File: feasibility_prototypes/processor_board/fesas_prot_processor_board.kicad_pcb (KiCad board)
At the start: 2 copper layers, 89 x 91 mm, 21 parts, among them P1 CONN_01X08, P10 CONN_01X02, P2 CONN_01X08, P3 CONN_01X02, P4 CONN_01X06, P5 CONN_01X08, P6 CONN_01X08, P7 CONN_01X08, P8 CONN_01X08, P9 CONN_01X02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

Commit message: Addded guard trace for cap-sense pad
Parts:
- added R5: R, Resistors_SMD:R_0805_HandSoldering, F.Cu at (197.5, 59.1)
- added R6: R, Resistors_SMD:R_0805_HandSoldering, F.Cu at (197.5, 66.7)
- added SW1: NKKswitches_G3T22AP, med_conn_prototype_footprints:NKKSwitches_G3T22AP, F.Cu at (191.8, 62.9)
- moved P9 14.5 mm to (181.0, 41.3)
- moved P4 12.1 mm to (198.8, 41.3)
- moved P10 7.85 mm to (172.7, 56.5)
- moved C3 4.58 mm to (191.8, 82.5)
- moved P2 3.81 mm to (191.8, 115.6)
- moved P5 3.81 mm to (161.3, 100.3)
- moved P1 1.27 mm to (125.7, 69.8)
- moved P3 0.63 mm to (160.0, 41.3)
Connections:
- U1 pad 27: /PGC(ICSPCLK) -> Net-(SW1-Pad2)
- U1 pad 28: /PGD(ICSPDAT) -> Net-(SW1-Pad5)
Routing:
- net /Guard_trace: track 0.00 -> 101.2 mm
- net Net-(SW1-Pad5): track 0.00 -> 31.4 mm
- net Net-(SW1-Pad2): track 0.00 -> 26.6 mm
- net /PGD(ICSPDAT): track 39.1 -> 23.2 mm
- net /MCLR/Vpp: track 74.3 -> 84.4 mm
- net Net-(P10-Pad2): track 25.8 -> 35.3 mm
- net /PGC(ICSPCLK): track 44.5 -> 35.8 mm
- net Net-(R5-Pad2): track 0.00 -> 8.19 mm
- net Net-(R6-Pad1): track 0.00 -> 6.91 mm
- net Net-(P2-Pad8): track 48.9 -> 53.4 mm
- net Net-(P2-Pad6): track 53.6 -> 58.0 mm
- net Net-(P2-Pad4): track 58.2 -> 62.7 mm
- net Net-(P5-Pad5): track 36.3 -> 40.1 mm
- net Net-(P5-Pad3): track 36.4 -> 40.2 mm
- net GND: track 57.4 -> 59.5 mm
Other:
- board size 89 x 91 mm -> 95 x 91 mm

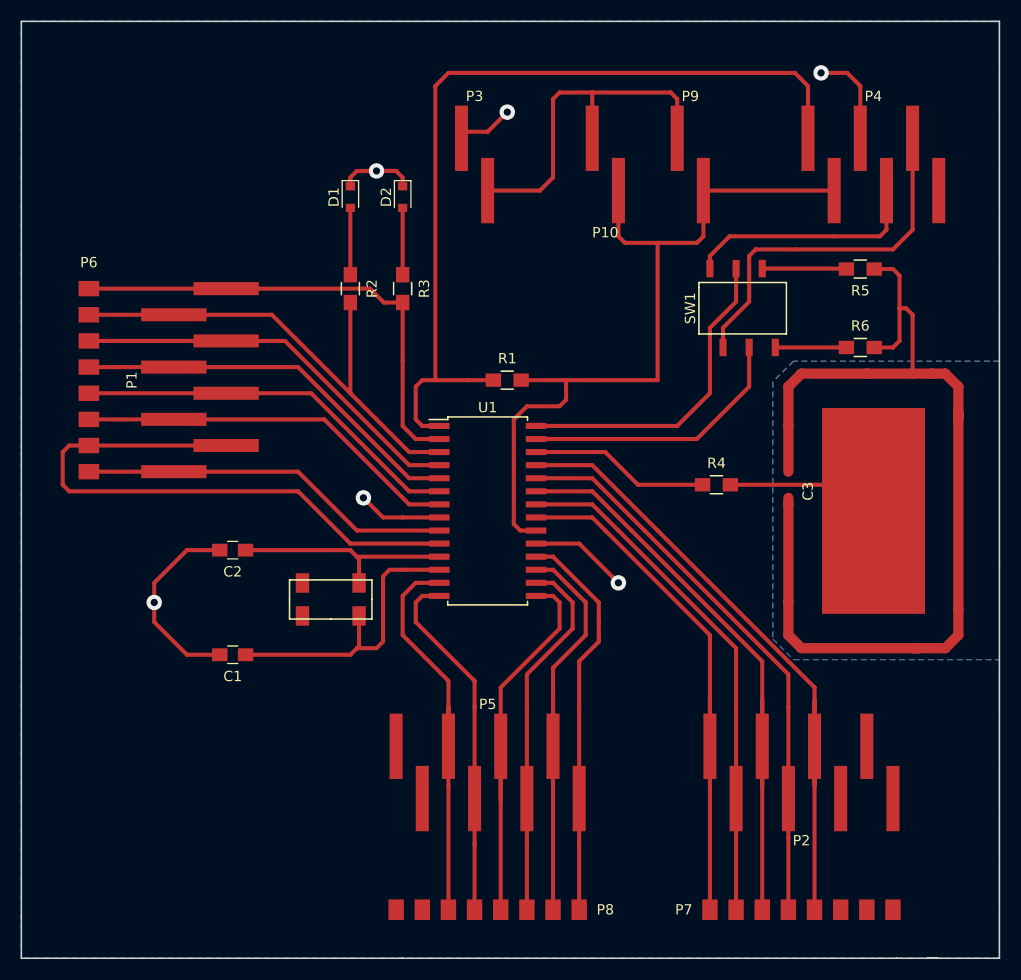
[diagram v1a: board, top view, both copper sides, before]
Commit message: Added RJ11 connector to processor board, finished IR board.
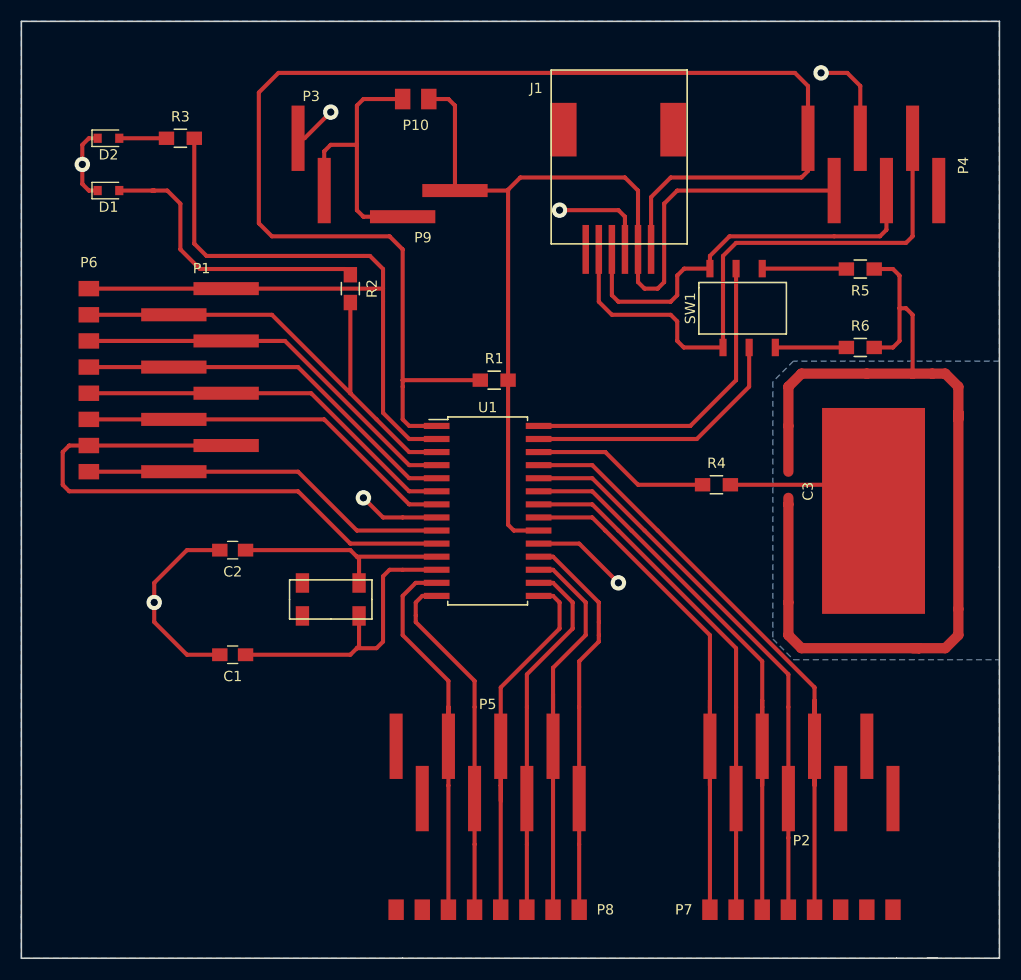
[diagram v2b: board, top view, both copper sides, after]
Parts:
- added J1: RJ11, med_conn_prototype_footprints:RJ11_SMD_Socket, F.Cu at (174.0, 54.6)
- P10: footprint med_conn_prototype_footprints:Sullins_SMD_pin_header_1x2_GBC36SABN-M30 -> med_conn_prototype_footprints:wire_solder_pad_2.54mm_1x2
- U1: footprint Housings_SOIC:SOIC-28W_7.5x17.9mm_Pitch1.27mm -> med_conn_prototype_footprints:SOIC-28W_7.5x17.9mm_Pitch1.27mm
- moved P9 34.9 mm to (148.0, 52.7), turned to 90 degrees
- moved D2 29.1 mm to (124.5, 46.4), turned to 0 degrees
- moved R3 26.1 mm to (131.4, 46.4), turned to 0 degrees
- moved D1 23.5 mm to (124.5, 51.4), turned to 0 degrees
- moved P10 21.0 mm to (154.3, 46.4)
- moved P3 15.9 mm to (144.1, 41.3)
- moved R1 1.27 mm to (161.9, 69.8)
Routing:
- net /MCLR/Vpp: track 84.4 -> 139.6 mm
- net Net-(P1-Pad8): track 46.5 -> 77.8 mm
- net VDD: track 76.7 -> 102.2 mm
- net Net-(D1-Pad2): track 6.49 -> 28.7 mm
- net /PGC(ICSPCLK): track 35.8 -> 57.7 mm
- net /PGD(ICSPDAT): track 23.2 -> 39.9 mm
- net Net-(P10-Pad2): track 35.3 -> 26.8 mm
- net GND: track 59.5 -> 67.2 mm, vias 6 -> 7
- net Net-(D2-Pad2): track 6.49 -> 4.58 mm
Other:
- outline, holes or cut-outs redrawn
